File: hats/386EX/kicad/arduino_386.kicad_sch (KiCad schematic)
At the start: 15 parts, among them J1 Conn_01x02_Pin, U11 I386EX_PQFP

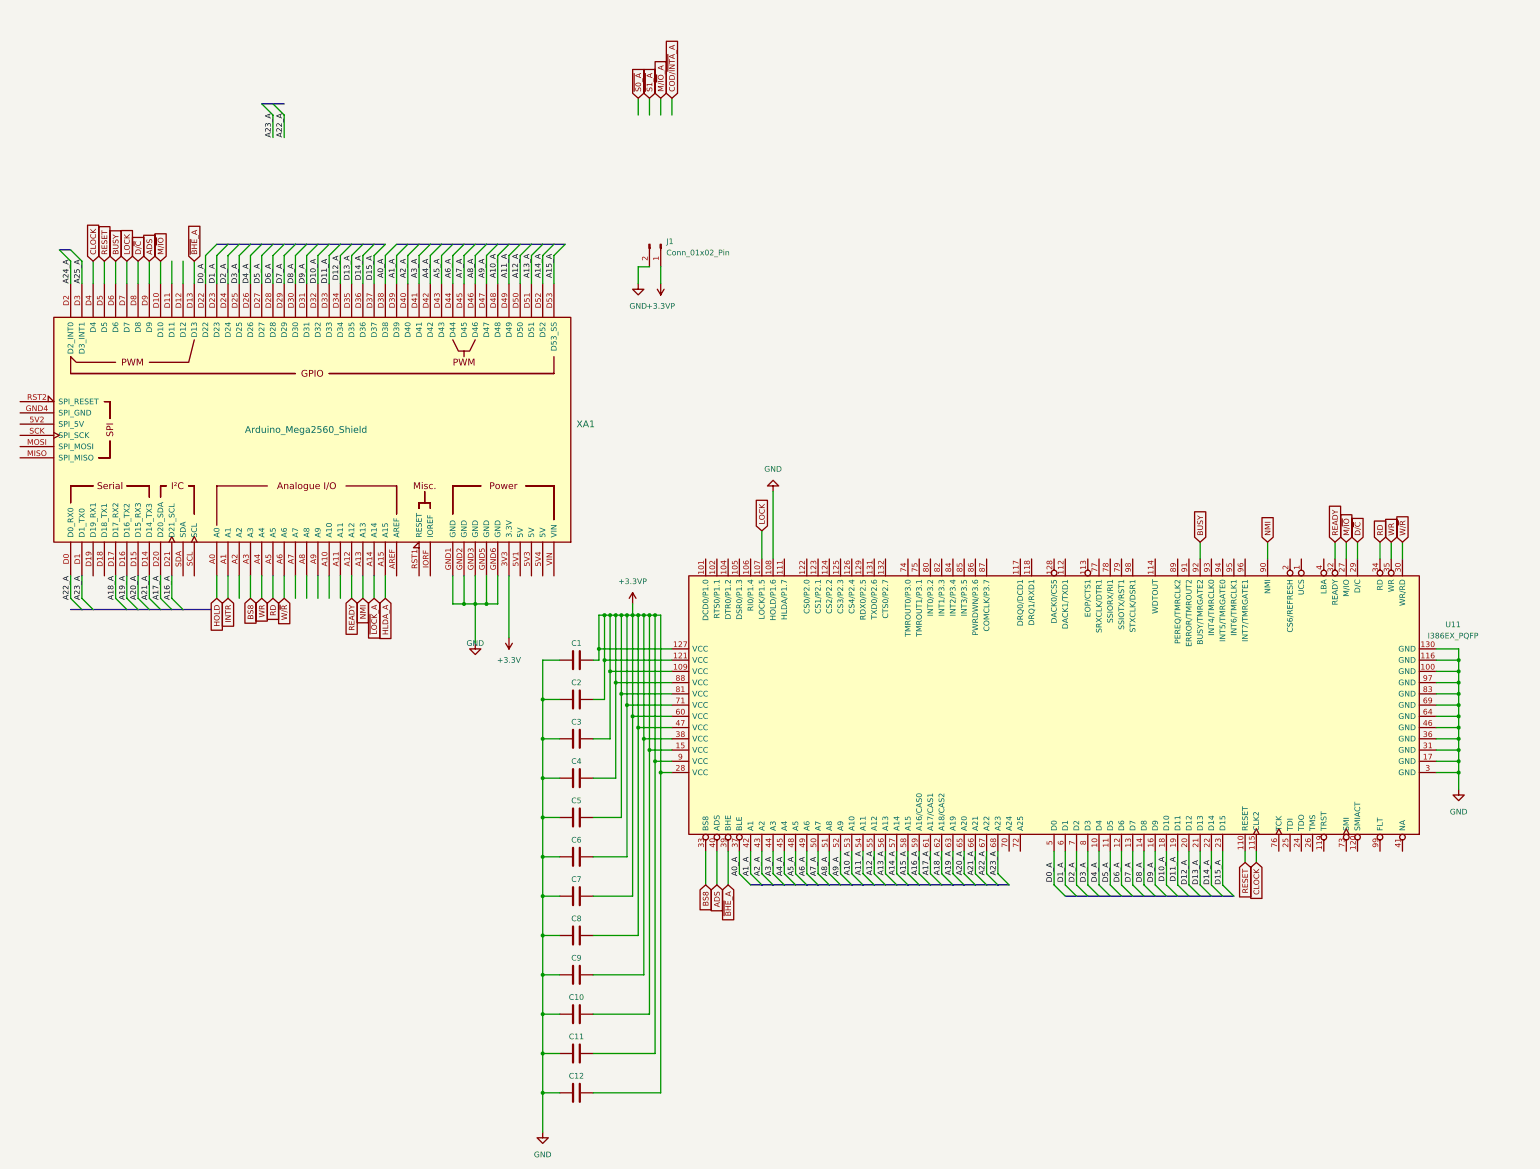
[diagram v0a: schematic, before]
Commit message: add JTAG header, connect SMI pins
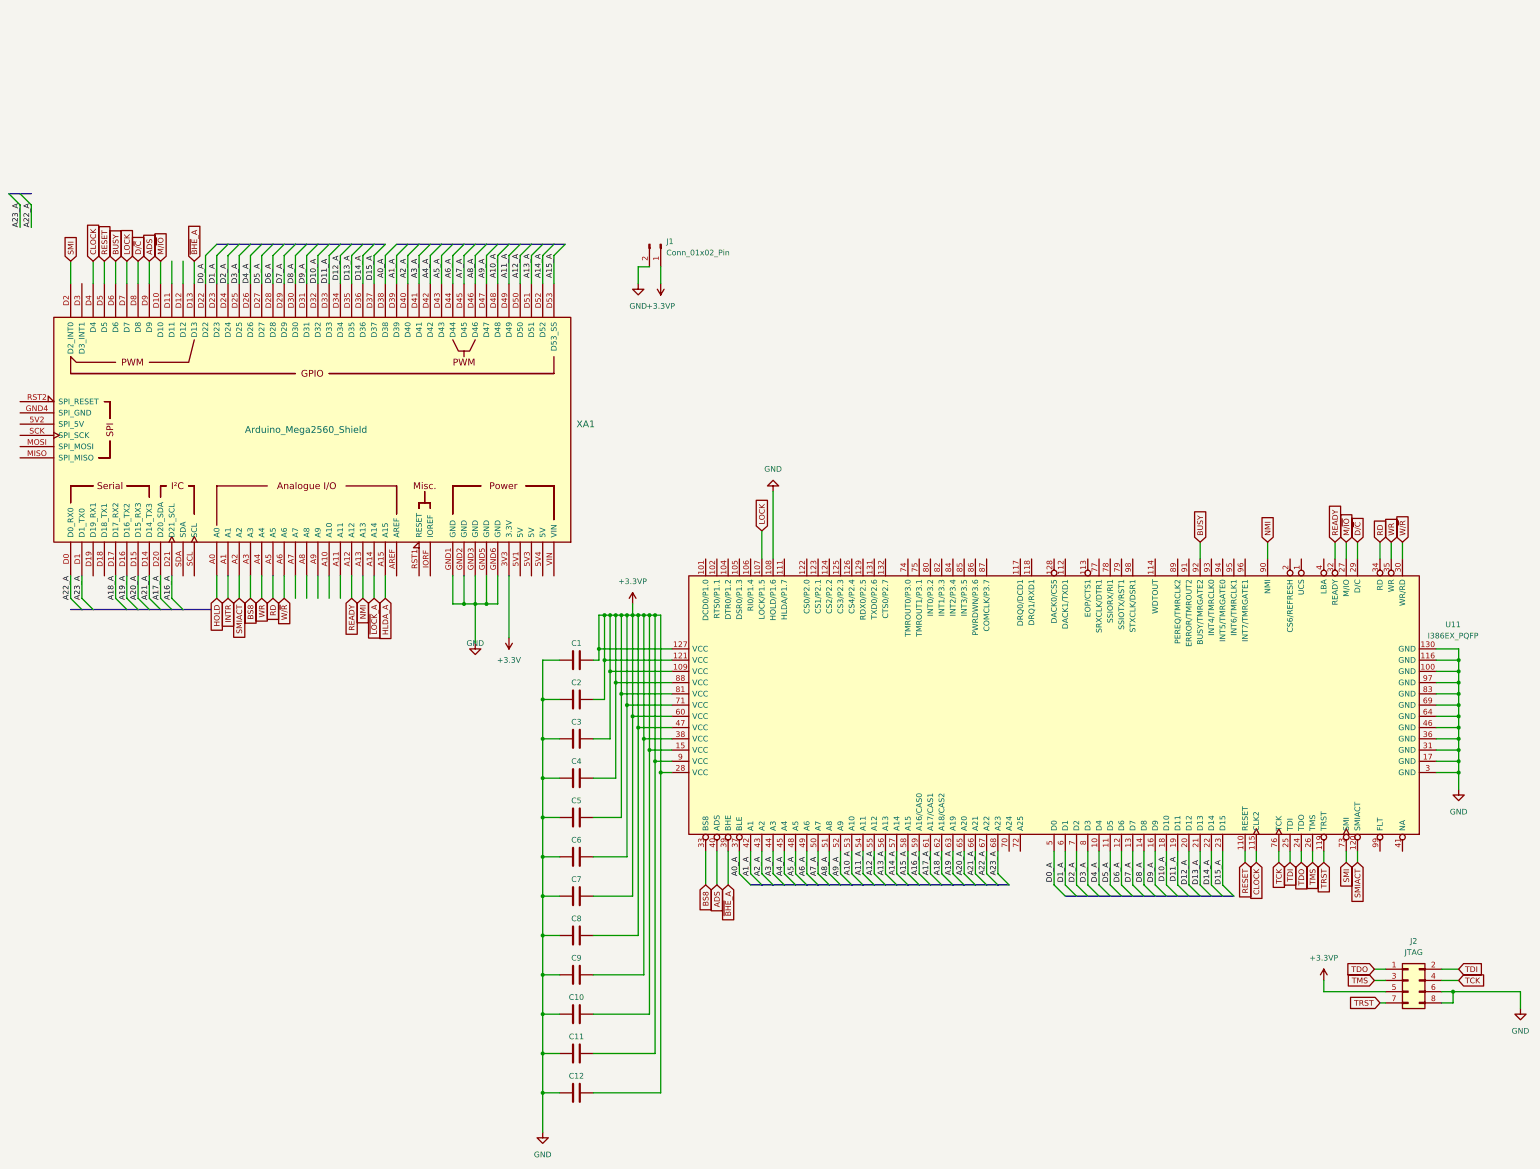
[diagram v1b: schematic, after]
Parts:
- added J2: JTAG, Connector_PinHeader_2.54mm:PinHeader_2x04_P2.54mm_Vertical, symbol Connector_Generic:Conn_02x04_Odd_Even
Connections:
- net A24_A is gone; now on net SMI: XA1.D2 (D2_INT0)
- net +3.3VP: now also J2.5 (Pin_5)
- net GND: now also J2.6 (Pin_6), J2.8 (Pin_8)
- net SMIACT: now reaches XA1.A2
- net SMIACT: now also U11.120 (SMIACT)
- net TRST: now reaches U11.119 (TRST)
- net TRST: now also J2.7 (Pin_7)
- net TDO: now reaches U11.24 (TDO)
- net TDO: now also J2.1 (Pin_1)
- net TDI: now reaches U11.25 (TDI)
- net TDI: now also J2.2 (Pin_2)
- net TMS: now reaches U11.26 (TMS)
- net TMS: now also J2.3 (Pin_3)
- net SMI: now reaches U11.73 (SMI)
- net TCK: now reaches U11.76 (TCK)
- net TCK: now also J2.4 (Pin_4)
- net A25_A: no longer names the net of XA1.D3 (D3_INT1)
